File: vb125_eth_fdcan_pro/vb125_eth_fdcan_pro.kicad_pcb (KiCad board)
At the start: 4 copper layers, 105 x 82 mm, 288 parts, among them J1 TAGconnect NL, J2 ARJM11C7-114-BA-EW2, J3 USB_C_Receptacle_USB2.0, J4 D09P33E4GL00LF, J5 D09P33E4GL00LF, J6 MEM2061-01-188-00-A, J7 Conn_02x20_Pin, K1 EE2-4.5TNUH, K2 EE2-4.5TNUH, M1 DM-OLED042-647, M2 B0505MT-1WR4, M3 B0505MT-1WR4, Q1 BSS138, Q2 BSS138, Q3 BSS138, Q4 BSS138, Q5 2N7002, Q6 MMBTA42, Q7 Si3440DV, SW1 KSS331GLFS, T1 PA1134NL, T2 750315125, U1 STM32H725IGKx, U10 PS2911-1-F3-AX, U11 ADM3050EBRIZ, U12 ZR431, U13 ADM3050EBRIZ, U14 TLP2270, U15 NCP563SQ18T1G, U2 LAN8740A, U3 USB3315, U4 LV14360SDDAR, U6 RT5760A/B, U7 LT8304IS8E#PBF, U8 TLP2270, U9 LTC4267, X1 50MHz, X2 24MHz

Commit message: Reimport parts onto PCB.
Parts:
- removed D5: CMZ5944B, Diode_SMD:D_SMA
- removed D8: HDS10M-13, vhrd_passive_diode:DIOB_HDS10M-13
- removed X1: 50MHz, Oscillator:Oscillator_SMD_Abracon_ASE-4Pin_3.2x2.5mm
- added D19: CMZ5944B, Diode_SMD:D_SMA, F.Cu at (116.6, 131.7)
- added D22: PDS360-13, Diode_SMD:D_PowerDI-5, F.Cu at (116.9, 122.0)
- added TP1: TestPoint_Probe, TestPoint:TestPoint_Pad_D1.5mm, F.Cu at (65.5, 46.5)
- added TP10: TestPoint_Probe, TestPoint:TestPoint_Pad_D1.5mm, F.Cu at (82.0, 148.4)
- added TP11: TestPoint_Probe, TestPoint:TestPoint_Pad_D1.5mm, F.Cu at (82.0, 151.9)
- added TP12: TestPoint_Probe, TestPoint:TestPoint_Pad_D1.5mm, F.Cu at (82.0, 155.5)
- added TP13: TestPoint_Probe, TestPoint:TestPoint_Pad_D1.5mm, F.Cu at (82.0, 159.0)
- added TP14: TestPoint_Probe, TestPoint:TestPoint_Pad_D1.5mm, F.Cu at (82.0, 162.6)
- added TP15: TestPoint_Probe, TestPoint:TestPoint_Pad_D1.5mm, F.Cu at (74.1, 132.2)
- added TP16: TestPoint_Probe, TestPoint:TestPoint_Pad_D1.5mm, F.Cu at (74.1, 135.7)
- added TP17: TestPoint_Probe, TestPoint:TestPoint_Pad_D1.5mm, F.Cu at (74.1, 139.3)
- added TP18: TestPoint_Probe, TestPoint:TestPoint_Pad_D1.5mm, F.Cu at (74.1, 142.8)
- added TP19: TestPoint_Probe, TestPoint:TestPoint_Pad_D1.5mm, F.Cu at (35.2, 132.2)
- added TP2: TestPoint_Probe, TestPoint:TestPoint_Pad_D1.5mm, F.Cu at (65.5, 50.1)
- added TP20: TestPoint_Probe, TestPoint:TestPoint_Pad_D1.5mm, F.Cu at (35.2, 135.7)
- added TP21: TestPoint_Probe, TestPoint:TestPoint_Pad_D1.5mm, F.Cu at (35.2, 139.3)
- added TP22: TestPoint_Probe, TestPoint:TestPoint_Pad_D1.5mm, F.Cu at (35.2, 142.8)
- added TP23: TestPoint_Probe, TestPoint:TestPoint_Pad_D1.5mm, F.Cu at (85.3, 46.5)
- added TP24: TestPoint_Probe, TestPoint:TestPoint_Pad_D1.5mm, F.Cu at (85.3, 50.1)
- added TP25: TestPoint_Probe, TestPoint:TestPoint_Pad_D1.5mm, F.Cu at (85.3, 53.6)
- added TP26: TestPoint_Probe, TestPoint:TestPoint_Pad_D1.5mm, F.Cu at (85.3, 57.2)
- added TP27: TestPoint_Probe, TestPoint:TestPoint_Pad_D1.5mm, F.Cu at (88.8, 46.5)
- added TP28: TestPoint_Probe, TestPoint:TestPoint_Pad_D1.5mm, F.Cu at (88.8, 50.1)
- added TP29: TestPoint_Probe, TestPoint:TestPoint_Pad_D1.5mm, F.Cu at (88.8, 53.6)
- added TP3: TestPoint_Probe, TestPoint:TestPoint_Pad_D1.5mm, F.Cu at (65.5, 53.6)
- added TP30: TestPoint_Probe, TestPoint:TestPoint_Pad_D1.5mm, F.Cu at (88.8, 57.2)
- added TP31: TestPoint_Probe, TestPoint:TestPoint_Pad_D1.5mm, F.Cu at (92.4, 46.5)
- added TP32: TestPoint_Probe, TestPoint:TestPoint_Pad_D1.5mm, F.Cu at (92.4, 50.1)
- added TP33: TestPoint_Probe, TestPoint:TestPoint_Pad_D1.5mm, F.Cu at (92.4, 53.6)
- added TP34: TestPoint_Probe, TestPoint:TestPoint_Pad_D1.5mm, F.Cu at (98.8, 115.4)
- added TP35: TestPoint_Probe, TestPoint:TestPoint_Pad_D1.5mm, F.Cu at (98.8, 118.9)
- added TP36: TestPoint_Probe, TestPoint:TestPoint_Pad_D1.5mm, F.Cu at (98.8, 122.5)
- added TP37: TestPoint_Probe, TestPoint:TestPoint_Pad_D1.5mm, F.Cu at (98.8, 126.0)
- added TP38: TestPoint_Probe, TestPoint:TestPoint_Pad_D1.5mm, F.Cu at (102.3, 115.4)
- added TP39: TestPoint_Probe, TestPoint:TestPoint_Pad_D1.5mm, F.Cu at (102.3, 118.9)
- added TP4: TestPoint_Probe, TestPoint:TestPoint_Pad_D1.5mm, F.Cu at (118.8, 151.6)
- added TP40: TestPoint_Probe, TestPoint:TestPoint_Pad_D1.5mm, F.Cu at (102.3, 122.5)
- added TP5: TestPoint_Probe, TestPoint:TestPoint_Pad_D1.5mm, F.Cu at (118.8, 155.2)
- added TP6: TestPoint_Probe, TestPoint:TestPoint_Pad_D1.5mm, F.Cu at (118.8, 158.7)
- added TP7: TestPoint_Probe, TestPoint:TestPoint_Pad_D1.5mm, F.Cu at (59.8, 158.4)
- added TP8: TestPoint_Probe, TestPoint:TestPoint_Pad_D1.5mm, F.Cu at (59.8, 161.9)
- added TP9: TestPoint_Probe, TestPoint:TestPoint_Pad_D1.5mm, F.Cu at (59.8, 165.5)
- added X3: 24MHz, Oscillator:Oscillator_SMD_Abracon_ASE-4Pin_3.2x2.5mm, F.Cu at (75.7, 158.8)
- C1: footprint Capacitor_SMD:C_0603_1608Metric -> Capacitor_SMD:C_0402_1005Metric
- C10: footprint Capacitor_SMD:C_0402_1005Metric -> Capacitor_SMD:C_0603_1608Metric
- C100: value 1uF -> 220uF?; footprint Capacitor_SMD:C_0402_1005Metric -> Capacitor_SMD:CP_Elec_6.3x7.7
- C101, C102: value Y rated, THT -> 4.7uF; footprint Capacitor_THT:C_Disc_D7.0mm_W2.5mm_P5.00mm -> Capacitor_SMD:C_1210_3225Metric
- C103: value Y rated, SMD 1808 -> 10uF; footprint vhrd_generic:C_1808_4520Metric -> Capacitor_SMD:C_1210_3225Metric
- C104: value Y rated, SMD 1808 -> 4.7uF; footprint vhrd_generic:C_1808_4520Metric -> Capacitor_SMD:C_1210_3225Metric
- C106: value 100nF -> 4.7uF; footprint Capacitor_SMD:C_0402_1005Metric -> Capacitor_SMD:C_1210_3225Metric
- C107, C109: value 4.7uF -> 100nF; footprint Capacitor_SMD:C_1210_3225Metric -> Capacitor_SMD:C_0402_1005Metric
- C108: value 4.7uF -> 1uF; footprint Capacitor_SMD:C_1210_3225Metric -> Capacitor_SMD:C_0402_1005Metric
- C110: value 4.7uF -> 220pF; footprint Capacitor_SMD:C_1210_3225Metric -> Capacitor_SMD:C_0603_1608Metric
- C111: value 100nF -> 100uF; footprint Capacitor_SMD:C_0402_1005Metric -> Capacitor_SMD:C_1210_3225Metric
- C113: value Y rated, THT -> 100uF; footprint Capacitor_THT:C_Disc_D7.0mm_W2.5mm_P5.00mm -> Capacitor_SMD:C_1210_3225Metric
- C114: value Y rated, SMD 1808 -> 100uF; footprint vhrd_generic:C_1808_4520Metric -> Capacitor_SMD:C_1210_3225Metric
- C12: value 2.2uF -> 100nF
- C14, C19, C32: value 4.7uF -> 100nF
- C15: value 10nF -> 4.7uF
- C16, C39: value 10nF -> 100nF
- C17: value 22nF -> 12pF
- C18, C37, C5: value 100nF -> 4.7uF
- C20: value 100nF -> 12pF
- C22, C25: value 100nF -> 1uF
- C27: value 100nF -> 10uF
- C3: value 100nF -> 2.2uF
- C30: value 1uF -> 220pF
- C31: value 4.7uF -> 10uF
- C33: value 220pF -> 100nF
- C34: value 10uF -> 100nF
- C35: value 10uF -> 1uF
- C36: value 1uF -> 470pF
- C40: value 10nF -> 22nF
- C41, C94: value 10nF -> 1uF
- C42: value 3.3nF -> 1uF
- C43: value >10uF -> 10nF; footprint Capacitor_SMD:C_0603_1608Metric -> Capacitor_SMD:C_0402_1005Metric
- C44: value DNP -> 4.7uF
- C45, C77, C82: value 100nF -> 10nF
- C46, C48: value 10uF -> 10nF; footprint Capacitor_SMD:C_0805_2012Metric -> Capacitor_SMD:C_0402_1005Metric
- C47: value DNP -> 100nF
- C49: value 1uF -> 10nF
- C50: value 220pF -> 100nF; footprint Capacitor_SMD:C_0603_1608Metric -> Capacitor_SMD:C_0402_1005Metric
- C51: value 4.7uF -> 1uF; footprint Capacitor_SMD:C_0603_1608Metric -> Capacitor_SMD:C_0402_1005Metric
- C52: value 4.7uF -> >10uF
- C53: value 4n7 -> 3.3nF
- C54: value 100nF -> DNP; footprint Capacitor_SMD:C_0402_1005Metric -> Capacitor_SMD:C_0603_1608Metric
- C55: value DNP -> 10uF
- C56, C75: value 10uF -> 100nF; footprint Capacitor_SMD:C_0805_2012Metric -> Capacitor_SMD:C_0402_1005Metric
- C57: value 10uF -> DNP; footprint Capacitor_SMD:C_0805_2012Metric -> Capacitor_SMD:C_0402_1005Metric
- C58: value 100nF -> 10uF; footprint Capacitor_SMD:C_0402_1005Metric -> Capacitor_SMD:C_0805_2012Metric
- C59: value 4.7uF -> DNP; footprint Capacitor_SMD:C_0603_1608Metric -> Capacitor_SMD:C_0805_2012Metric
- C60: value 10nF -> 10uF; footprint Capacitor_SMD:C_0402_1005Metric -> Capacitor_SMD:C_0805_2012Metric
- C62, C76: value 10nF -> 4.7uF; footprint Capacitor_SMD:C_0402_1005Metric -> Capacitor_SMD:C_0603_1608Metric
- C63: value 4.7uF -> 10nF; footprint Capacitor_SMD:C_1210_3225Metric -> Capacitor_SMD:C_0402_1005Metric
- C64: value 100nF -> 4.7uF; footprint Capacitor_SMD:C_0805_2012Metric -> Capacitor_SMD:C_0603_1608Metric
- C65: value 1uF -> Y rated, THT; footprint Capacitor_SMD:C_1210_3225Metric -> Capacitor_THT:C_Disc_D7.0mm_W2.5mm_P5.00mm
- C66: value 47uF -> Y rated, SMD 1808; footprint Capacitor_SMD:C_1210_3225Metric -> vhrd_generic:C_1808_4520Metric
- C67: value 47uF -> 100nF; footprint Capacitor_SMD:C_1210_3225Metric -> Capacitor_SMD:C_0402_1005Metric
- C68: value 220uF? -> 10nF; footprint Capacitor_SMD:CP_Elec_6.3x7.7 -> Capacitor_SMD:C_0402_1005Metric
- C69: value 33nF -> 10uF; footprint Capacitor_SMD:C_0402_1005Metric -> Capacitor_SMD:C_0805_2012Metric
- C7: value 470pF -> 1uF
- C70, C9: value 1uF -> 100nF
- C71: value 27nF -> 10uF; footprint Capacitor_SMD:C_0402_1005Metric -> Capacitor_SMD:C_0805_2012Metric
- C72: value 470pF -> 4n7
- C73: value 68pF -> DNP; footprint Capacitor_SMD:C_0603_1608Metric -> Capacitor_SMD:C_0805_2012Metric
- C74: value 4.7uF -> 10uF; footprint Capacitor_SMD:C_0603_1608Metric -> Capacitor_SMD:C_0805_2012Metric
- C78: value DNP -> 4.7uF; footprint Capacitor_SMD:C_0805_2012Metric -> Capacitor_SMD:C_0603_1608Metric
- C79: value 10uF -> Y rated, THT; footprint Capacitor_SMD:C_0805_2012Metric -> Capacitor_THT:C_Disc_D7.0mm_W2.5mm_P5.00mm
- C8: value 1uF -> 4.7uF; footprint Capacitor_SMD:C_0402_1005Metric -> Capacitor_SMD:C_0603_1608Metric
- C80: value 10uF -> Y rated, SMD 1808; footprint Capacitor_SMD:C_1210_3225Metric -> vhrd_generic:C_1808_4520Metric
- C81: value 4.7uF -> 100nF; footprint Capacitor_SMD:C_0603_1608Metric -> Capacitor_SMD:C_0402_1005Metric
- C83: value 12pF -> 10uF; footprint Capacitor_SMD:C_0402_1005Metric -> Capacitor_SMD:C_0805_2012Metric
- C84: value 12pF -> 100nF
- C85: value 1uF -> 10uF; footprint Capacitor_SMD:C_0402_1005Metric -> Capacitor_SMD:C_0805_2012Metric
- C86: value 100nF -> 4n7
- C87: footprint Capacitor_SMD:C_0603_1608Metric -> Capacitor_SMD:C_1210_3225Metric
- C88: footprint Capacitor_SMD:C_0402_1005Metric -> Capacitor_SMD:C_0805_2012Metric
- C89: value 100uF -> 1uF
- C90: value 100uF -> 4.7uF; footprint Capacitor_SMD:C_1210_3225Metric -> Capacitor_SMD:C_0603_1608Metric
- C91: value 100uF -> 68pF; footprint Capacitor_SMD:C_1210_3225Metric -> Capacitor_SMD:C_0603_1608Metric
- C92: value 4.7uF -> Y rated, THT; footprint Capacitor_SMD:C_0603_1608Metric -> Capacitor_THT:C_Disc_D7.0mm_W2.5mm_P5.00mm
- C93: value 100nF -> Y rated, SMD 1808; footprint Capacitor_SMD:C_0402_1005Metric -> vhrd_generic:C_1808_4520Metric
- C95: value 10uF -> 47uF; footprint Capacitor_SMD:C_0805_2012Metric -> Capacitor_SMD:C_1210_3225Metric
- C96: value 100nF -> 470pF
- C97: value 10uF -> 33nF; footprint Capacitor_SMD:C_0805_2012Metric -> Capacitor_SMD:C_0402_1005Metric
- C98: value 4n7 -> 47uF; footprint Capacitor_SMD:C_0402_1005Metric -> Capacitor_SMD:C_1210_3225Metric
- C99: value 1uF -> 27nF
- D10: value SMAJ58A -> HDS10M-13; footprint Diode_SMD:D_SMA -> vhrd_passive_diode:DIOB_HDS10M-13
- D11: value PDS360-13 -> SMAJ58A; footprint Diode_SMD:D_PowerDI-5 -> Diode_SMD:D_SMA
- D12: value BAS516 -> MMSZ5237BS-7-F; footprint Diode_SMD:D_SOD-523 -> Diode_SMD:D_SOD-323
- D14: value MMSZ5237BS-7-F -> BAS516; footprint Diode_SMD:D_SOD-323 -> Diode_SMD:D_SOD-523
- D16: value BAS516 -> PDS360-13; footprint Diode_SMD:D_SOD-523 -> Diode_SMD:D_PowerDI-5
- D17: value BAS516 -> buspower_iso: SMAJ58CA; buspower_dc: SMAJ36CA; footprint Diode_SMD:D_SOD-523 -> Diode_SMD:D_SMA
- D18: value BAS516 -> RB168MM150TFTR; footprint Diode_SMD:D_SOD-523 -> Diode_SMD:D_SOD-123F
- D21: value buspower_iso: SMAJ58CA; buspower_dc: SMAJ36CA -> PDS360-13; footprint Diode_SMD:D_SMA -> Diode_SMD:D_PowerDI-5
- D23: value PDS360-13 -> 5V6?; footprint Diode_SMD:D_PowerDI-5 -> Diode_SMD:D_SOD-323
- D3: value 5V6? -> BAS516; footprint Diode_SMD:D_SOD-323 -> Diode_SMD:D_SOD-523
- D4: value RB168MM150TFTR -> BAS516; footprint Diode_SMD:D_SOD-123F -> Diode_SMD:D_SOD-523
- D6: value PDS360-13 -> BAS516; footprint Diode_SMD:D_PowerDI-5 -> Diode_SMD:D_SOD-523
- D7: value HDS10M-13 -> BAS516; footprint vhrd_passive_diode:DIOB_HDS10M-13 -> Diode_SMD:D_SOD-523
- D9: value BAS516 -> HDS10M-13; footprint Diode_SMD:D_SOD-523 -> vhrd_passive_diode:DIOB_HDS10M-13
- FB1: value MH1608-601Y -> FBMJ1608HM180NTR
- FB2: value FBMJ1608HM180NTR -> MH1608-601Y
- J1: value TAGconnect NL -> MEM2061-01-188-00-A; footprint vhrd_connector_debug:TC2050-IDC-NL -> vhrd_connector_gct:MEM2061
- J2: value ARJM11C7-114-BA-EW2 -> TAGconnect NL; footprint vhrd_connector_abracon:RJ45_Abracon_ARJM11_7POE_LED -> vhrd_connector_debug:TC2050-IDC-NL
- J3: value USB_C_Receptacle_USB2.0 -> Conn_02x20_Pin; footprint Connector_USB:USB_C_Receptacle_GCT_USB4105-xx-A_16P_TopMnt_Horizontal -> Connector_PinHeader_1.27mm:PinHeader_2x20_P1.27mm_Vertical_SMD
- J4: value D09P33E4GL00LF -> ARJM11C7-114-BA-EW2; footprint vhrd_connector_amphenol:D09P33E4GL00LF -> vhrd_connector_abracon:RJ45_Abracon_ARJM11_7POE_LED
- J5: value D09P33E4GL00LF -> USB_C_Receptacle_USB2.0; footprint vhrd_connector_amphenol:D09P33E4GL00LF -> Connector_USB:USB_C_Receptacle_GCT_USB4105-xx-A_16P_TopMnt_Horizontal
- J6: value MEM2061-01-188-00-A -> D09P33E4GL00LF; footprint vhrd_connector_gct:MEM2061 -> vhrd_connector_amphenol:D09P33E4GL00LF
- J7: value Conn_02x20_Pin -> D09P33E4GL00LF; footprint Connector_PinHeader_1.27mm:PinHeader_2x20_P1.27mm_Vertical_SMD -> vhrd_connector_amphenol:D09P33E4GL00LF
- K1, K2: footprint vhrd_relay:Relay_DPDT_Kemet_EE2_NUH_DoubleCoil -> Relay_SMD:Relay_DPDT_Kemet_EE2_NUH_DoubleCoil
- L3: value 3.3uH -> 6.8uH
- L5: value 6.8uH -> 3.3uH
- M1: moved to F.Cu
- Q5: value 2N7002 -> MMBTA42
- Q6: value MMBTA42 -> Si3440DV; footprint Package_TO_SOT_SMD:SOT-23 -> Package_SO:TSOP-6_1.65x3.05mm_P0.95mm
- Q7: value Si3440DV -> 2N7002; footprint Package_SO:TSOP-6_1.65x3.05mm_P0.95mm -> Package_TO_SOT_SMD:SOT-23
- R1: value 10K -> 3K3
- R10, R2, R3, R4, R5, R6, R8, R9: value 10k -> 3K3
- R11: value 33R -> 3K3
- R12, R13: value 33R -> 10K
- R14, R23: value 10k -> 33R
- R15: value 10k -> 49R9
- R16: value 10k -> 0
- R17: value 12k1 -> 10K
- R18: value 10k -> 10K
- R19, R20, R24, R26: value ?R -> 10k
- R21: value ?R -> 33R
- R22: value 49R9 -> 33R
- R25: value ?R -> 1k5
- R27, R29, R30: value 49R9 -> 10k
- R28: value 49R9 -> 12k1
- R31, R32: value 1K -> 10k
- R33: value 0 -> 10k
- R34, R47: value 10K -> 10k
- R35: value 10K -> 49R9
- R36: value 5K1 -> 49R9
- R37: value 5K1 -> 10k
- R38: value 39R -> 49R9
- R39: value 301K -> 49R9
- R40: value 0 -> ?R
- R41, R42: value 100K -> ?R
- R43: value 45k -> 1K
- R44: value 10k -> 1K
- R45: value 1M -> 5K1
- R46: value 348K -> 5K1
- R48: value ?R -> 39R
- R49: value 158K -> 39R
- R50: value 100R -> ?R
- R51, R52: value 60R4 -> 10K; footprint Resistor_SMD:R_0603_1608Metric -> Resistor_SMD:R_0402_1005Metric
- R53, R54: value 1K -> ?R
- R55: value 1K -> 0
- R56: value 1K -> 301K
- R57, R58: value 60R4 -> 100K; footprint Resistor_SMD:R_0603_1608Metric -> Resistor_SMD:R_0402_1005Metric
- R59: value 3K3 -> 45k
- R60: value 3K3 -> 10k
- R61, R62, R83: value 3K3 -> 1K
- R63, R64: value DNP -> 60R4; footprint Resistor_SMD:R_0402_1005Metric -> Resistor_SMD:R_0603_1608Metric
- R65: value DNP -> 1K
- R66: value 470R -> 1K
- R67: value 100K -> 60R4; footprint Resistor_SMD:R_0402_1005Metric -> Resistor_SMD:R_0603_1608Metric
- R68: value 33K2 -> 60R4; footprint Resistor_SMD:R_0402_1005Metric -> Resistor_SMD:R_0603_1608Metric
- R69: value 47K -> DNP
- R7: value 1k5 -> 10K
- R70: value 1K -> DNP
- R71: value 10K -> DNP
- R72: value 6K8 -> DNP
- R73: value 100K -> 220K
- R74: value 10R -> 220K; footprint Resistor_SMD:R_0603_1608Metric -> Resistor_SMD:R_0402_1005Metric
- R75: value DNP -> 10K
- R76: value 510R -> 100K
- R77: value 0.125R -> 100R; footprint Resistor_SMD:R_1206_3216Metric -> Resistor_SMD:R_0805_2012Metric
- R78: value 100R -> 4K7; footprint Resistor_SMD:R_0805_2012Metric -> Resistor_SMD:R_0402_1005Metric
- R79: value 4K7 -> 0.125R; footprint Resistor_SMD:R_0402_1005Metric -> Resistor_SMD:R_1206_3216Metric
- R80: value 220K -> 6K8
- R81: value 220K -> 510R
- R82: value 3K3 -> 10R; footprint Resistor_SMD:R_0402_1005Metric -> Resistor_SMD:R_0603_1608Metric
- R84: value 3K3 -> 470R
- R85: value 3K3 -> 47K
- R86: value 3K3 -> 100K
- R87: value 3K3 -> 33K2
- R88: value 33R -> 49K9
- R89: value 10K -> 1M
- R90: value 10K -> 348K
- R92: value 39R -> ?R
- R94: value 250R -> 100R; footprint Resistor_SMD:R_0603_1608Metric -> Resistor_SMD:R_0402_1005Metric
- R95: value 10K -> 158K
- R96: value 49K9 -> 57K6
- R98: value 57K6 -> 250R; footprint Resistor_SMD:R_0402_1005Metric -> Resistor_SMD:R_0603_1608Metric
- U10: value PS2911-1-F3-AX -> TLP2270; footprint vhrd_opto_isolator:PS2911 -> vhrd_generic:SO8L_TOS
- U11: value ADM3050EBRIZ -> LTC4267; footprint vhrd_generic:RI-8-1_ADI -> Package_DFN_QFN:DFN-16-1EP_3x5mm_P0.5mm_EP1.66x4.4mm
- U12: value ZR431 -> PS2911-1-F3-AX; footprint Package_TO_SOT_SMD:SOT-23 -> Package_DIP:DIP-4_W7.62mm
- U13: value ADM3050EBRIZ -> ZR431; footprint vhrd_generic:RI-8-1_ADI -> Package_TO_SOT_SMD:SOT-23
- U14: value TLP2270 -> LV14360SDDAR; footprint vhrd_generic:SO8L_TOS -> Package_SO:SOIC-8-1EP_3.9x4.9mm_P1.27mm_EP2.95x4.9mm_Mask2.71x3.4mm_ThermalVias
- U15: value NCP563SQ18T1G -> LT8304IS8E#PBF; footprint Package_TO_SOT_SMD:SC-82AB -> vhrd_generic:SOIC-8-ANALOG
- U3: value USB3315 -> NCP563SQ18T1G; footprint vhrd_interface_usb:QFN24_MICROCHIP -> Package_TO_SOT_SMD:SC-82AB
- U4: value LV14360SDDAR -> USB3315; footprint Package_SO:SOIC-8-1EP_3.9x4.9mm_P1.27mm_EP2.95x4.9mm_Mask2.71x3.4mm_ThermalVias -> vhrd_interface_usb:QFN24_MICROCHIP
- U7: value LT8304IS8E#PBF -> ADM3050EBRIZ; footprint vhrd_generic:SOIC-8-ANALOG -> vhrd_generic:RI-8-1_ADI
- U9: value LTC4267 -> ADM3050EBRIZ; footprint Package_DFN_QFN:DFN-16-1EP_3x5mm_P0.5mm_EP1.66x4.4mm -> vhrd_generic:RI-8-1_ADI
- X2: value 24MHz -> 50MHz
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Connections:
- C100 pad 1: /USB/+1V8_ULPI -> +5V0_SYS
- C101 pad 1: GND -> /Bus Power/+VIN_DB9_PR
- C101 pad 2: /CAN Ch1/ISO -> ISO_1
- C102 pad 1: GND -> /Bus Power/+VIN_DB9_PR
- C102 pad 2: /CAN Ch2/ISO -> ISO_1
- C103 pad 1: GND -> /Bus Power/+VIN_DB9_PR
- C103 pad 2: /CAN Ch1/ISO -> ISO_1
- C104 pad 1: GND -> /Bus Power/+VIN_DB9_PR
- C104 pad 2: /CAN Ch2/ISO -> ISO_1
- C106 pad 1: /Bus Power/LV_SS -> /Bus Power/+VIN_DB9_PR
- C107 pad 1: /Bus Power/+VIN_DB9_PR -> /Bus Power/LV_SS
- C108 pad 1: /Bus Power/+VIN_DB9_PR -> /Bus Power/BP_INT_VCC
- C109 pad 1: /Bus Power/+VIN_DB9_PR -> /Bus Power/LV_BOOT
- C109 pad 2: ISO_1 -> /Bus Power/LV_SW
- C110 pad 2: ISO_1 -> Net-(C110-Pad2)
- C111 pad 1: /Bus Power/LV_BOOT -> /Bus Power/+5V0_BP_DC
- C111 pad 2: /Bus Power/LV_SW -> ISO_1
- C112 pad 1: /Bus Power/+5V0_BP_DC -> +5V0_SYS
- C112 pad 2: ISO_1 -> GND
- C113 pad 1: ISO_POE -> +5V0_SYS
- C114 pad 1: ISO_POE -> +5V0_SYS
- C12 pad 1: /MCU_H7/+VCOMH_OLED -> +3V3_DCDC
- C13 pad 1: /MCU_H7/+VCC_OLED -> +3V3_DCDC
- C14 pad 1: /MCU_H7/+VCC_OLED -> +3V3_DCDC
- C15 pad 1: +3V3_DCDC -> /MCU_H7/VCAP
- C17 pad 1: /Eth/+AVDD_PHY -> /MCU_H7/OSC32_IN
- C18 pad 1: /Eth/+AVDD_PHY -> /MCU_H7/VCAP
- C19 pad 1: /Eth/+AVDD_PHY -> +3V3_DCDC
- C20 pad 1: +3V3_DCDC -> /MCU_H7/OSC32_OUT
- C22 pad 1: +3V3_DCDC -> /MCU_H7/VDDA
- C24 pad 1: +3V3_DCDC -> /MCU_H7/VDDA
- C27 pad 1: +3V3_DCDC -> /MCU_H7/VDDSMPS
- C29 pad 1: /MCU_H7/VDDA -> /MCU_H7/~{H7_RST}
- C3 pad 1: /Eth/+AVDD_PHY -> /MCU_H7/+VCOMH_OLED
- C30 pad 1: /MCU_H7/VDDA -> /MCU_H7/VLX
- C31 pad 1: /MCU_H7/VCAP -> /MCU_H7/VDDLDO
- C32 pad 1: /MCU_H7/VCAP -> +3V3_DCDC
- C33 pad 1: /MCU_H7/VLX -> /Eth/+AVDD_PHY
- C34 pad 1: /MCU_H7/VDDSMPS -> /Eth/+AVDD_PHY
- C35 pad 1: /MCU_H7/VDDLDO -> /Eth/VDDCR_PHY
- C36 pad 1: +3V3_DCDC -> /Eth/VDDCR_PHY
- C37 pad 1: /MCU_H7/~{H7_RST} -> /Eth/+AVDD_PHY
- C38 pad 1: +VIN_USB -> +3V3_DCDC
- C39 pad 1: +VIN_USB -> /Eth/+AVDD_PHY
- C4 pad 1: /Eth/+AVDD_PHY -> /MCU_H7/+VCC_OLED
- C40 pad 1: +VIN_USB -> /Eth/+AVDD_PHY
- C41 pad 1: +VIN_USB -> +3V3_DCDC
- C42 pad 1: /Power/AOZ_SS -> /USB/+1V8_ULPI
- C44 pad 1: +5V0_SYS -> +3V3_DCDC
- C45 pad 1: +5V0_SYS -> +3V3_DCDC
- C46 pad 1: +5V0_SYS -> +VIN_USB
- C47 pad 2: /Power/3V3_FB -> GND
- C48 pad 1: +3V3_DCDC -> +VIN_USB
- C49 pad 1: /Bus Power/BP_INT_VCC -> +VIN_USB
- C49 pad 2: ISO_1 -> GND
- C5 pad 1: +3V3_DCDC -> /MCU_H7/+VCC_OLED
- C50 pad 1: /Bus Power/+VIN_DB9_PR -> /USB/+1V8_ULPI
- C50 pad 2: Net-(C50-Pad2) -> GND
- C51 pad 1: Net-(C51-Pad1) -> /USB/ULPI_REGOUT_3V3
- C52 pad 1: +5V0_SYS -> +VIN_USB
- C53 pad 1: Net-(C53-Pad1) -> /Power/AOZ_SS
- C53 pad 2: /CAN Ch1/ISO -> GND
- C54 pad 1: /CAN Ch1/+5V0_ISO -> +5V0_SYS
- C54 pad 2: /CAN Ch1/ISO -> GND
- C55 pad 1: +3V3_DCDC -> +5V0_SYS
- C56 pad 1: Net-(U11-VDD1) -> +5V0_SYS
- C57 pad 1: /CAN Ch1/+VO -> +3V3_DCDC
- C57 pad 2: /CAN Ch1/ISO -> /Power/3V3_FB
- C58 pad 1: Net-(U11-VDD1) -> +3V3_DCDC
- C59 pad 1: +5V0_SYS -> +3V3_DCDC
- C6 pad 1: /Eth/VDDCR_PHY -> Net-(M1-C2P)
- C6 pad 2: GND -> Net-(M1-C2N)
- C60 pad 1: Net-(U11-VDD1) -> Net-(U7-VDD1)
- C61 pad 1: Net-(U13-VDD1) -> Net-(U7-VDD1)
- C62 pad 1: Net-(U13-VDD1) -> +5V0_SYS
- C63 pad 1: /PoE/POE_BR_P -> Net-(U7-VDD1)
- C63 pad 2: /PoE/POE_BR_N -> GND
- C64 pad 1: /PoE/POE_BR_P -> Net-(C64-Pad1)
- C64 pad 2: /PoE/POE_BR_N -> GND
- C65 pad 1: /PoE/POE_VPORTP -> GND
- C65 pad 2: ISO_POE -> ISO_1
- C66 pad 1: +5V0_SYS -> GND
- C66 pad 2: GND -> ISO_1
- C67 pad 1: +5V0_SYS -> /CAN Ch1/+5V0_ISO
- C67 pad 2: GND -> ISO_1
- C68 pad 1: +5V0_SYS -> /CAN Ch1/+5V0_ISO
- C68 pad 2: GND -> ISO_1
- C69 pad 1: /PoE/POE_COMP -> /CAN Ch1/+VO
- C69 pad 2: /PoE/POE_OP_A -> ISO_1
- C7 pad 1: /Eth/VDDCR_PHY -> Net-(M1-C1P)
- C7 pad 2: GND -> Net-(M1-C1N)
- C70 pad 1: /PoE/POE_COMP -> /CAN Ch1/+5V0_ISO
- C70 pad 2: GND -> ISO_1
- C71 pad 1: Net-(C71-Pad1) -> /CAN Ch1/+5V0_ISO
- C71 pad 2: /PoE/POE_OP_K -> ISO_1
- C72 pad 2: +5V0_SYS -> ISO_1
- C73 pad 1: /PoE/POE_VPORTP -> +3V3_DCDC
- C73 pad 2: Net-(C73-Pad2) -> GND
- C74 pad 1: /PoE/POE_PVCC -> Net-(U9-VDD1)
- C74 pad 2: ISO_POE -> GND
- C75 pad 1: Net-(U13-VDD1) -> Net-(U9-VDD1)
- C76 pad 1: /CAN Ch1/+5V0_ISO -> +5V0_SYS
- C76 pad 2: /CAN Ch1/ISO -> GND
- C77 pad 1: /CAN Ch1/+5V0_ISO -> Net-(U9-VDD1)
- C77 pad 2: /CAN Ch1/ISO -> GND
- C78 pad 1: +3V3_DCDC -> Net-(C78-Pad1)
- C79 pad 1: /CAN Ch1/+5V0_ISO -> GND
- C79 pad 2: /CAN Ch1/ISO -> /CAN Ch2/ISO
- C8 pad 1: Net-(M1-C2P) -> +3V3_DCDC
- C8 pad 2: Net-(M1-C2N) -> GND
- C80 pad 1: /Bus Power/+VIN_DB9_PR -> GND
- C80 pad 2: ISO_1 -> /CAN Ch2/ISO
- C81 pad 1: +3V3_DCDC -> /CAN Ch2/+5V0_ISO
- C81 pad 2: GND -> /CAN Ch2/ISO
- C82 pad 1: +3V3_DCDC -> /CAN Ch2/+5V0_ISO
- C82 pad 2: GND -> /CAN Ch2/ISO
- C83 pad 1: /MCU_H7/OSC32_OUT -> /CAN Ch2/+VO
- C83 pad 2: GND -> /CAN Ch2/ISO
- C84 pad 1: /MCU_H7/OSC32_IN -> /CAN Ch2/+5V0_ISO
- C84 pad 2: GND -> /CAN Ch2/ISO
- C85 pad 1: /USB/ULPI_REGOUT_3V3 -> /CAN Ch2/+5V0_ISO
- C85 pad 2: GND -> /CAN Ch2/ISO
- C86 pad 1: /USB/+1V8_ULPI -> Net-(C86-Pad1)
- C86 pad 2: GND -> /CAN Ch2/ISO
- C87 pad 1: +3V3_DCDC -> /PoE/POE_BR_P
- C87 pad 2: GND -> /PoE/POE_BR_N
- C88 pad 1: +3V3_DCDC -> /PoE/POE_BR_P
- C88 pad 2: GND -> /PoE/POE_BR_N
- C89 pad 1: +5V0_SYS -> /PoE/POE_VPORTP
- C89 pad 2: GND -> ISO_POE
- C9 pad 1: Net-(M1-C1P) -> +3V3_DCDC
- C9 pad 2: Net-(M1-C1N) -> GND
- C90 pad 1: +5V0_SYS -> /PoE/POE_PVCC
- C90 pad 2: GND -> ISO_POE
- C91 pad 1: +5V0_SYS -> /PoE/POE_VPORTP
- C91 pad 2: GND -> Net-(C91-Pad2)
- C92 pad 1: Net-(C92-Pad1) -> ISO_POE
- C93 pad 1: /CAN Ch2/+5V0_ISO -> ISO_POE
- C93 pad 2: /CAN Ch2/ISO -> GND
- C94 pad 1: /CAN Ch2/+5V0_ISO -> /PoE/POE_COMP
- C94 pad 2: /CAN Ch2/ISO -> GND
- C95 pad 1: /CAN Ch2/+VO -> +5V0_SYS
- C95 pad 2: /CAN Ch2/ISO -> GND
- C96 pad 1: /CAN Ch2/+5V0_ISO -> Net-(C96-Pad1)
- C96 pad 2: /CAN Ch2/ISO -> +5V0_SYS
- C97 pad 1: /CAN Ch2/+5V0_ISO -> /PoE/POE_COMP
- C97 pad 2: /CAN Ch2/ISO -> /PoE/POE_OP_A
- C98 pad 1: Net-(C98-Pad1) -> +5V0_SYS
- C98 pad 2: /CAN Ch2/ISO -> GND
- C99 pad 1: +3V3_DCDC -> Net-(C99-Pad1)
- C99 pad 2: GND -> /PoE/POE_OP_K
- D10 pad 2: /PoE/POE_BR_N -> POE_AC4
- D11 pad 1: +5V0_SYS -> /PoE/POE_BR_P
- D11 pad 2: Net-(D11-A) -> /PoE/POE_BR_N
- D13 pad 1: Net-(D13-K) -> /PoE/POE_PVCC
- D13 pad 2: /PoE/POE_ITH -> Net-(D13-A)
- D15 pad 1: /CAN Ch1/+5V0_ISO -> Net-(D15-K)
- D15 pad 2: Net-(D15-A) -> /PoE/POE_ITH
- D16 pad 1: /CAN Ch1/+5V0_ISO -> +5V0_SYS
- D17 pad 1: /CAN Ch2/+5V0_ISO -> CHASSIS
- D17 pad 2: Net-(D17-A) -> /Bus Power/+VIN_DB9
- D18 pad 1: /CAN Ch2/+5V0_ISO -> /Bus Power/+VIN_DB9_PR
- D18 pad 2: Net-(D18-A) -> /Bus Power/+VIN_DB9
- D20 pad 1: /Bus Power/+VIN_DB9_PR -> Net-(D19-K)
- D20 pad 2: /Bus Power/+VIN_DB9 -> /Bus Power/BP_SW
- D21 pad 1: CHASSIS -> /Bus Power/LV_SW
- D21 pad 2: /Bus Power/+VIN_DB9 -> ISO_1
- D23 pad 1: /Bus Power/LV_SW -> +5V0_SYS
- D23 pad 2: ISO_1 -> GND
- D3 pad 1: +5V0_SYS -> /CAN Ch1/+5V0_ISO
- D3 pad 2: GND -> Net-(D3-A)
- D4 pad 1: Net-(D4-K) -> /CAN Ch1/+5V0_ISO
- D4 pad 2: /Bus Power/BP_SW -> Net-(D4-A)
- D6 pad 1: +5V0_SYS -> /CAN Ch2/+5V0_ISO
- D7 pad 1: /PoE/POE_BR_P -> /CAN Ch2/+5V0_ISO
- D7 pad 2: POE_AC2 -> Net-(D7-A)
- D9 pad 1: /PoE/POE_PVCC -> /PoE/POE_BR_P
- D9 pad 2: Net-(D9-A) -> POE_AC2
- FB1 pad 2: /Eth/+AVDD_PHY -> /MCU_H7/VDDSMPS
- FB2 pad 2: /MCU_H7/VDDSMPS -> /Eth/+AVDD_PHY
- FB3 pad 2: Net-(U13-VDD1) -> Net-(U7-VDD1)
- FB5 pad 2: Net-(U11-VDD1) -> Net-(U9-VDD1)
- J1 pad 1: Net-(J1-Pad1) -> /MCU_H7/SDMMC_D2
- J1 pad 10: /MCU_H7/~{H7_RST} -> /MCU_H7/SDMMC_PRESENT
- J1 pad 2: /MCU_H7/H7_SWDIO -> /MCU_H7/SDMMC_D3
- J1 pad 3: GND -> /MCU_H7/SDMMC_CMD
- J1 pad 4: /MCU_H7/H7_SWCLK -> +3V3_DCDC
- J1 pad 5: GND -> /MCU_H7/SDMMC_CKJ
- J1 pad 6: unconnected-(J1-Pad6) -> GND
- J1 pad 7: unconnected-(J1-Pad7) -> /MCU_H7/SDMMC_D0
- J1 pad 8: /MCU_H7/BOOT0 -> /MCU_H7/SDMMC_D1
- J2 pad 1: POE_AC4 -> Net-(J2-Pad1)
- J2 pad 10: Net-(D1-I/O_3) -> /MCU_H7/~{H7_RST}
- J2 pad 2: POE_AC2 -> /MCU_H7/H7_SWDIO
- J2 pad 3: Net-(D1-I/O_1) -> GND
- J2 pad 4: /Eth/+AVDD_PHY -> /MCU_H7/H7_SWCLK
- J2 pad 5: Net-(D1-I/O_4) -> GND
- J2 pad 6: POE_AC3 -> unconnected-(J2-Pad6)
- J2 pad 7: POE_AC1 -> unconnected-(J2-Pad7)
- J2 pad 8: Net-(D1-I/O_2) -> /MCU_H7/BOOT0
- J2 pad 9: /Eth/+AVDD_PHY -> GND
- J4 pad 1: /Bus Power/+VIN_DB9 -> POE_AC4
- J4 pad 2: /CAN Ch1/CAN_L -> POE_AC2
- J4 pad 3: /CAN Ch1/ISO -> Net-(D1-I/O_1)
- J4 pad 4: unconnected-(J4-Pad4) -> /Eth/+AVDD_PHY
- J4 pad 5: unconnected-(J4-Pad5) -> Net-(D1-I/O_4)
- J4 pad 6: /CAN Ch1/ISO -> POE_AC3
- J4 pad 7: /CAN Ch1/CAN_H -> POE_AC1
- J4 pad 8: unconnected-(J4-Pad8) -> Net-(D1-I/O_2)
- J4 pad 9: /Bus Power/+VIN_DB9 -> /Eth/+AVDD_PHY
- J6 pad 1: /MCU_H7/SDMMC_D2 -> /Bus Power/+VIN_DB9
- J6 pad 2: /MCU_H7/SDMMC_D3 -> /CAN Ch1/CAN_L
- J6 pad 3: /MCU_H7/SDMMC_CMD -> ISO_1
- J6 pad 4: +3V3_DCDC -> unconnected-(J6-Pad4)
- J6 pad 5: /MCU_H7/SDMMC_CKJ -> unconnected-(J6-Pad5)
- J6 pad 6: GND -> ISO_1
- J6 pad 7: /MCU_H7/SDMMC_D0 -> /CAN Ch1/CAN_H
- J6 pad 8: /MCU_H7/SDMMC_D1 -> unconnected-(J6-Pad8)
- J6 pad 9: GND -> /Bus Power/+VIN_DB9
- J7 pad 1: /MCU_H7/SPI1_SCK -> /CAN Ch2/+VIN_DB9
- J7 pad 2: /MCU_H7/OCTOSPI_IO0 -> /CAN Ch2/CAN_L
- J7 pad 3: GND -> /CAN Ch2/ISO
- J7 pad 4: /MCU_H7/OCTOSPI_IO1 -> unconnected-(J7-Pad4)
- J7 pad 5: /MCU_H7/SPI1_MISO -> unconnected-(J7-Pad5)
- J7 pad 6: /MCU_H7/OCTOSPI_IO2 -> /CAN Ch2/ISO
- J7 pad 7: /MCU_H7/SPI1_MOSI -> /CAN Ch2/CAN_H
- J7 pad 8: /MCU_H7/OCTOSPI_IO3 -> unconnected-(J7-Pad8)
- J7 pad 9: /MCU_H7/SPI1_NSS -> /CAN Ch2/+VIN_DB9
- K1 pad 12: Net-(D15-A) -> Net-(D3-A)
- K1 pad 4: Net-(C53-Pad1) -> Net-(C72-Pad1)
- K1 pad 7: Net-(D16-A) -> Net-(D4-A)
- K1 pad 9: Net-(C53-Pad1) -> Net-(C72-Pad1)
- K2 pad 12: Net-(D17-A) -> Net-(D6-A)
- K2 pad 4: Net-(C98-Pad1) -> Net-(C86-Pad1)
- K2 pad 7: Net-(D18-A) -> Net-(D7-A)
- K2 pad 9: Net-(C98-Pad1) -> Net-(C86-Pad1)
- L3 pad 1: /PoE/POE_BR_P -> +5V0_SYS
- L3 pad 2: /PoE/POE_VPORTP -> Net-(C64-Pad1)
- L4 pad 2: Net-(C51-Pad1) -> Net-(C78-Pad1)
- L5 pad 1: +5V0_SYS -> /PoE/POE_BR_P
- L5 pad 2: Net-(C92-Pad1) -> /PoE/POE_VPORTP
- M2 pad 13: Net-(C51-Pad1) -> Net-(C64-Pad1)
- M2 pad 14: Net-(C51-Pad1) -> Net-(C64-Pad1)
- M2 pad 6: /CAN Ch1/ISO -> ISO_1
- M2 pad 7: /CAN Ch1/ISO -> ISO_1
- M3 pad 13: Net-(C92-Pad1) -> Net-(C78-Pad1)
- M3 pad 14: Net-(C92-Pad1) -> Net-(C78-Pad1)
- Q1 pad 1: /CAN Ch2/CT_GS -> /CAN Ch1/CT_GS
- Q1 pad 2: /CAN Ch2/ISO -> ISO_1
- Q1 pad 3: Net-(D17-A) -> Net-(D3-A)
- Q2 pad 1: /CAN Ch2/CT_GR -> /CAN Ch1/CT_GR
- Q2 pad 2: /CAN Ch2/ISO -> ISO_1
- Q2 pad 3: Net-(D18-A) -> Net-(D4-A)
- Q3 pad 1: /CAN Ch1/CT_GS -> /CAN Ch2/CT_GS
- Q3 pad 2: /CAN Ch1/ISO -> /CAN Ch2/ISO
- Q3 pad 3: Net-(D15-A) -> Net-(D6-A)
- Q4 pad 1: /CAN Ch1/CT_GR -> /CAN Ch2/CT_GR
- Q4 pad 2: /CAN Ch1/ISO -> /CAN Ch2/ISO
- Q4 pad 3: Net-(D16-A) -> Net-(D7-A)
- Q5 pad 2: ISO_POE -> /PoE/POE_PVCC
- Q5 pad 3: /PoE/POE_ITH -> /PoE/POE_VPORTP
- Q6 pad 1: Net-(D14-K) -> /PoE/POE_TR_SW
- Q6 pad 2: /PoE/POE_PVCC -> /PoE/POE_TR_SW
- Q6 pad 3: /PoE/POE_VPORTP -> Net-(Q6-G)
- Q7 pad 1: /PoE/POE_TR_SW -> Net-(D14-K)
- Q7 pad 2: /PoE/POE_TR_SW -> ISO_POE
- Q7 pad 3: Net-(Q7-G) -> /PoE/POE_ITH
- R1 pad 2: Net-(M1-BS1) -> /MCU_H7/I2C2_SDA
- R10 pad 1: GND -> +3V3_DCDC
- R10 pad 2: /Eth/TXD3_NU -> /MCU_H7/RID_BOM
- R11 pad 1: ETH_CRS_DV -> /MCU_H7/RID_BOM
- R11 pad 2: Net-(U2A-COL/CRS_DV/MODE2) -> GND
- R12 pad 1: ETH_RXD0 -> +3V3_DCDC
- R12 pad 2: /Eth/RXD0 -> /MCU_H7/BUTTON
- R13 pad 1: ETH_RXD1 -> +3V3_DCDC
- R13 pad 2: /Eth/RXD1 -> /MCU_H7/SDMMC_PRESENT
- R14 pad 1: /Eth/PHYAD1 -> /MCU_H7/SDMMC_CK
- R14 pad 2: GND -> /MCU_H7/SDMMC_CKJ
- R15 pad 1: /Eth/PHYAD2 -> +3V3_DCDC
- R15 pad 2: GND -> Net-(J2-Pad1)
- R16 pad 1: /Eth/PHYAD0 -> +3V3_DCDC
- R16 pad 2: GND -> /MCU_H7/VDDA
- R17 pad 1: /Eth/RBIAS -> +3V3_DCDC
- R17 pad 2: GND -> Net-(U1I-PDR_ON)
- R18 pad 1: Net-(X1-EN) -> /MCU_H7/BOOT0
- R18 pad 2: +3V3_DCDC -> GND
- R19 pad 1: Net-(X1-OUT) -> GND
- R19 pad 2: Net-(R19-Pad2) -> /Eth/TXD2_NU
- R2 pad 2: Net-(U2A-~{INT}/TXER/TXD4) -> /MCU_H7/I2C2_SCL
- R20 pad 1: Net-(R19-Pad2) -> GND
- R20 pad 2: Net-(U2A-XTAL1/CLKIN) -> /Eth/TXD3_NU
- R21 pad 1: Net-(R19-Pad2) -> ETH_RXD0
- R21 pad 2: ETH_REFCLK -> /Eth/RXD0
- R22 pad 1: +3V3_DCDC -> ETH_RXD1
- R22 pad 2: Net-(J1-Pad1) -> /Eth/RXD1
- R23 pad 1: Net-(X2-EN) -> ETH_CRS_DV
- R23 pad 2: +3V3_DCDC -> Net-(U2A-COL/CRS_DV/MODE2)
- R24 pad 1: Net-(X2-OUT) -> +3V3_DCDC
- R24 pad 2: Net-(R24-Pad2) -> Net-(U2A-COL/CRS_DV/MODE2)
- R25 pad 1: Net-(R24-Pad2) -> +3V3_DCDC
- R25 pad 2: Net-(U3-REFCLK) -> ETH_MDIO
- R26 pad 1: Net-(R24-Pad2) -> +3V3_DCDC
- R26 pad 2: H7_CLK -> ~{ETH_PHY_RST}
- R27 pad 1: /Eth/+AVDD_PHY -> +3V3_DCDC
- R27 pad 2: Net-(D1-I/O_1) -> /Eth/RXD1
- R28 pad 1: /Eth/+AVDD_PHY -> /Eth/RBIAS
- R28 pad 2: Net-(D1-I/O_4) -> GND
- R29 pad 1: /Eth/+AVDD_PHY -> +3V3_DCDC
- R29 pad 2: Net-(D1-I/O_2) -> /Eth/RXD0
- R3 pad 2: /Eth/RXD2_NU -> /MCU_H7/I2C3_SDA
- R30 pad 1: /Eth/+AVDD_PHY -> +3V3_DCDC
- R30 pad 2: Net-(D1-I/O_3) -> /Eth/RXD2_NU
- R31 pad 1: Net-(J2-GA) -> /Eth/PHYAD0
- R31 pad 2: RJ45_LEDG -> GND
- R32 pad 1: Net-(J2-YA) -> +3V3_DCDC
- R32 pad 2: RJ45_LEDY -> Net-(U2A-~{INT}/TXER/TXD4)
- R33 pad 1: +3V3_DCDC -> /Eth/PHYAD2
- R33 pad 2: /MCU_H7/VDDA -> GND
- R34 pad 1: /MCU_H7/BOOT0 -> /Eth/PHYAD1
- R35 pad 1: +3V3_DCDC -> /Eth/+AVDD_PHY
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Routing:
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
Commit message: Preliminary floorplan
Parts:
- moved C52 188.9 mm to (235.4, 34.8)
- moved C53 188.9 mm to (239.2, 28.5)
- moved C54 188.9 mm to (235.4, 37.3)
- moved C55 188.9 mm to (235.6, 29.0)
- moved C56 188.9 mm to (239.2, 30.5)
- moved C57 188.9 mm to (239.2, 32.5)
- moved C58 188.9 mm to (235.6, 32.0)
- moved L2 188.9 mm to (235.8, 40.4)
- moved R55 188.9 mm to (231.9, 28.5)
- moved R56 188.9 mm to (231.9, 30.5)
- moved R57 188.9 mm to (231.9, 32.5)
- moved R59 188.9 mm to (231.9, 36.5)
- moved R60 188.9 mm to (231.9, 38.5)
- moved TP10 188.9 mm to (228.7, 29.3)
- moved TP11 188.9 mm to (228.7, 32.9)
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
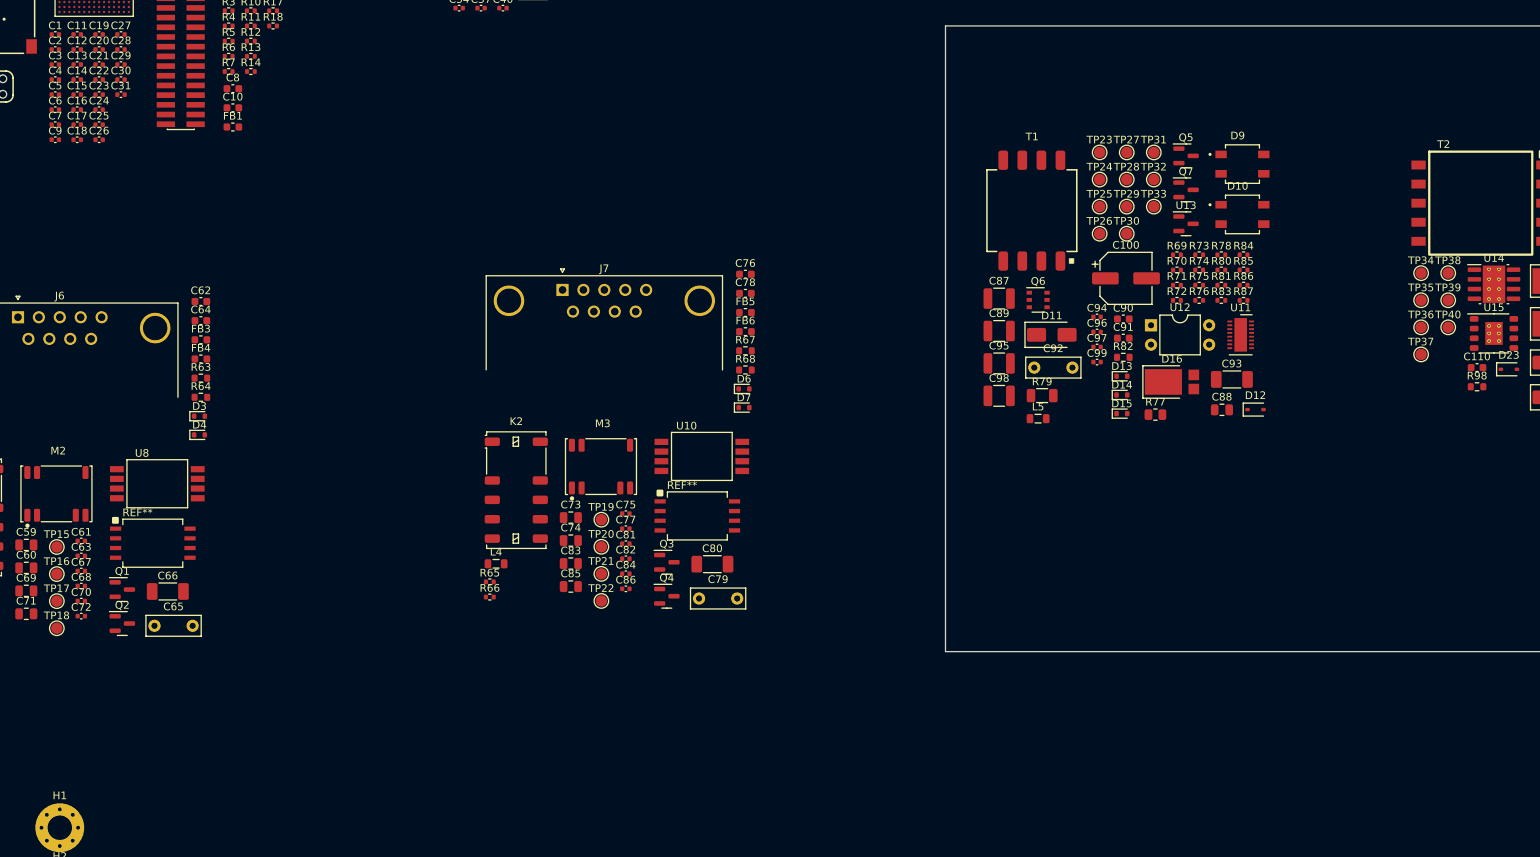
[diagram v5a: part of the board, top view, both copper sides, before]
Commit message: Add missing footprints, ready to layout.
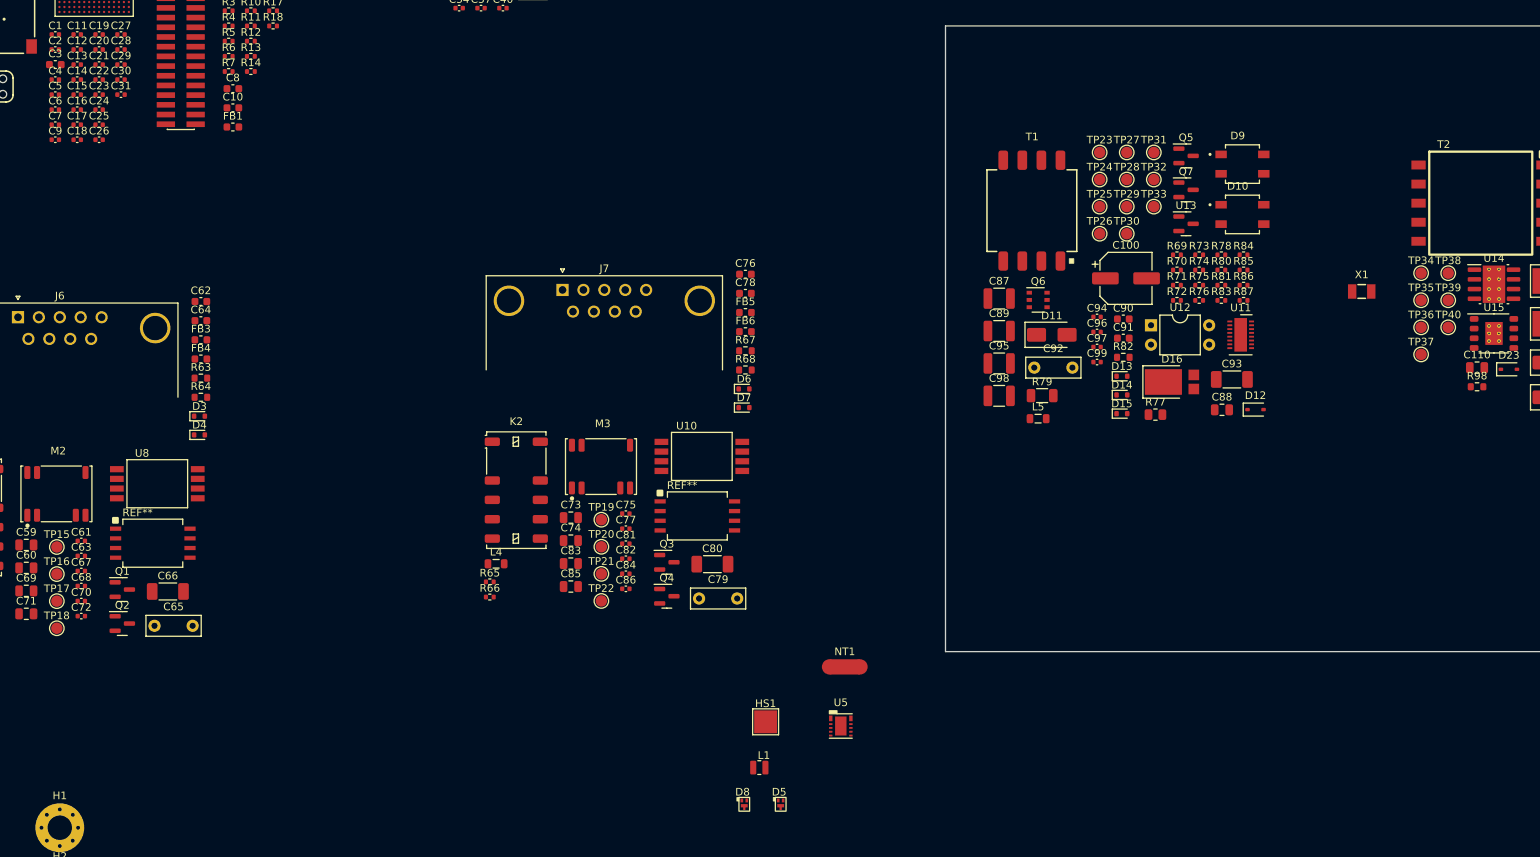
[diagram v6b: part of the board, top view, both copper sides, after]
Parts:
- added D5: PESD2CANFD24V-QBZ, vhrd_passive_diode:DFN1110D-3_3-XDFN, F.Cu at (137.8, 154.4)
- added D8: PESD2CANFD24V-QBZ, vhrd_passive_diode:DFN1110D-3_3-XDFN, F.Cu at (133.0, 154.4)
- added HS1: Heatsink_Pad, TestPoint:TestPoint_Pad_3.0x3.0mm, F.Cu at (135.8, 143.6)
- added L1: LQM2MPN2R2NG0, vhrd_inductor:MURATA_LQM2, F.Cu at (135.0, 149.6)
- added NT1: NetTie_2, NetTie:NetTie-2_SMD_Pad2.0mm, F.Cu at (146.2, 136.4)
- added U5: AOZ1376DI-02, vhrd_generic:DFN-12-AOZ, F.Cu at (145.7, 144.2)
- added X1: ECX-.327-CDX-1293, vhrd_crystal:ECX-.327-CDX-1293, F.Cu at (213.9, 87.2)
- B1: value BAT-HLD-001-THM -> (none)
- C110: footprint Capacitor_SMD:C_0603_1608Metric -> Capacitor_SMD:C_0805_2012Metric
- C3: footprint Capacitor_SMD:C_0402_1005Metric -> Capacitor_SMD:C_0603_1608Metric
- R10, R5, R8: value 3K3 -> 100K
- R11: value 3K3 -> RID_BOM
- R6: value 3K3 -> RID_PRODUCT
- R9: value 3K3 -> RID_REV
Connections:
- R10 pad 1: +3V3_DCDC -> /MCU_H7/RID_EN
- R5 pad 1: +3V3_DCDC -> /MCU_H7/RID_EN
- R8 pad 1: +3V3_DCDC -> /MCU_H7/RID_EN
- T2 pad 1: (no net) -> unconnected-(T2-NC-Pad1)
- T2 pad 2: (no net) -> unconnected-(T2-NC-Pad2)
- T2 pad 4: (no net) -> unconnected-(T2-NC-Pad4)
- T2 pad 8: (no net) -> unconnected-(T2-NC-Pad8)
- U1 pad P5: unconnected-(U1A-PA4-PadP5) -> /MCU_H7/RID_EN

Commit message: Preliminary placement.
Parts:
- removed C98: 47uF, Capacitor_SMD:C_1210_3225Metric
- removed D16: PDS360-13, Diode_SMD:D_PowerDI-5
- C10, C11, C12, C13, C14, C16, C19, C21, C22, C23, C24, C26, C27, C28, FB1, HS1, J1: moved to B.Cu
- C95: value 47uF -> 4.7uF; footprint Capacitor_SMD:C_1210_3225Metric -> Capacitor_SMD:C_0402_1005Metric
- J4: value ARJM11C7-114-BA-EW2 -> ARJM11D7-114-AB; footprint vhrd_connector_abracon:RJ45_Abracon_ARJM11_7POE_LED -> vhrd_connector_abracon:ARJM11D7-114-AB-EW2
- K1, K2: footprint Relay_SMD:Relay_DPDT_Kemet_EE2_NUH_DoubleCoil -> vhrd_relay:Relay_DPDT_Kemet_EE2_NUH_DoubleCoil
- M1: footprint vhrd_opto_display:DM-OLED042-647 -> vhrd_opto_display:DM-OLED042-647-TOP
- U12: footprint Package_DIP:DIP-4_W7.62mm -> vhrd_opto_isolator:PS2911
- moved TP10 209.4 mm to (21.1, 57.1)
- moved TP11 209.4 mm to (21.1, 60.6)
- moved TP12 209.4 mm to (21.1, 64.2)
- moved TP13 209.4 mm to (21.1, 67.8)
- moved TP14 209.4 mm to (21.1, 71.3)
- moved C62 196.8 mm to (257.7, 69.4)
- moved C64 196.8 mm to (257.7, 71.9)
- moved FB3 196.8 mm to (257.7, 74.4)
- moved FB4 196.8 mm to (257.7, 76.9)
- moved R63 196.8 mm to (257.7, 79.4)
- moved R64 196.8 mm to (257.7, 82.0)
- moved D3 196.8 mm to (257.5, 84.4)
- moved D4 196.8 mm to (257.5, 86.9)
- moved C59 196.7 mm to (229.7, 72.4)
- moved C60 196.7 mm to (229.7, 75.4)
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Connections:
- net Net-(D1-I/O_1) renamed /Eth/RD-
- net Net-(D1-I/O_2) renamed /Eth/TD-
- net Net-(D1-I/O_3) renamed /Eth/TD+
- net Net-(D1-I/O_4) renamed /Eth/RD+
- C15 pad 1: /MCU_H7/VCAP -> /MCU_H7/VDDLDO
- C18 pad 1: /MCU_H7/VCAP -> /MCU_H7/VDDLDO
- C95 pad 1: +5V0_SYS -> /MCU_H7/VDDLDO
- D22 pad 2: Net-(D22-A) -> /Bus Power/RECT_COMMON
- R43 pad 2: RJ45_LEDY -> RJ45_LEDG
- R44 pad 2: RJ45_LEDG -> RJ45_LEDY
- R82 pad 1: Net-(D16-A) -> /Bus Power/RECT_COMMON
- T1 pad 5: Net-(D16-A) -> /Bus Power/RECT_COMMON
- T1 pad 6: Net-(D16-A) -> /Bus Power/RECT_COMMON
- T2 pad 6: Net-(D22-A) -> /Bus Power/RECT_COMMON
- T2 pad 7: Net-(D22-A) -> /Bus Power/RECT_COMMON
- U1 pad A14: /MCU_H7/VCAP -> /MCU_H7/VDDLDO
- U1 pad A4: /MCU_H7/VCAP -> /MCU_H7/VDDLDO
- U1 pad R13: /MCU_H7/VCAP -> /MCU_H7/VDDLDO
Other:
- outline, holes or cut-outs redrawn

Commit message: Update vb125_eth_fdcan_pro.kicad_pcb
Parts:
- moved C32 115.9 mm to (129.7, 90.9), turned to -90 degrees
- moved R19 111.2 mm to (133.9, 84.1), turned to 180 degrees
- moved C33 111.0 mm to (129.6, 80.8), turned to 90 degrees
- moved R26 110.2 mm to (133.9, 86.1), turned to 180 degrees
- moved R20 109.3 mm to (133.9, 82.9), turned to 180 degrees
- moved R23 108.9 mm to (131.9, 90.9), turned to 90 degrees
- moved R21 108.9 mm to (128.6, 90.9), turned to 90 degrees
- moved R24 108.6 mm to (133.0, 90.9), turned to 90 degrees
- moved C37 108.5 mm to (130.6, 80.8), turned to 90 degrees
- moved R25 108.3 mm to (134.1, 90.9), turned to 90 degrees
- moved C40 107.7 mm to (132.6, 80.8), turned to 90 degrees
- moved C39 107.5 mm to (131.6, 80.8), turned to 90 degrees
- moved C34 106.0 mm to (123.7, 84.1), turned to 180 degrees
- moved R22 105.9 mm to (126.4, 90.9), turned to 90 degrees
- moved C35 105.8 mm to (123.7, 86.1), turned to 180 degrees
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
